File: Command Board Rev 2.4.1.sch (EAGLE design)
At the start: 44 parts, among them IC1 PIC24FXXKA302_SPDIP, Q2-IRF510 IRF740

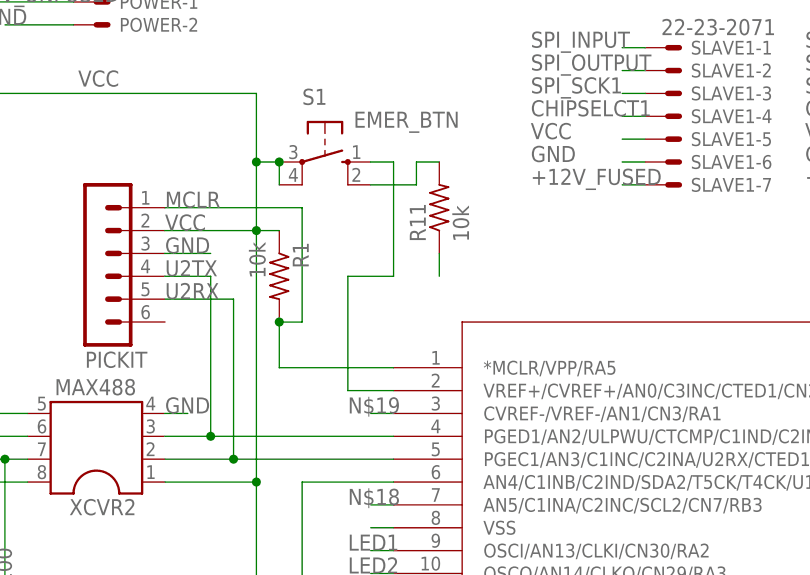
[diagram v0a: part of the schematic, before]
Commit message: Remove 2.4, Add 2.4.1
Replaces 2.4 files with 2.4.1
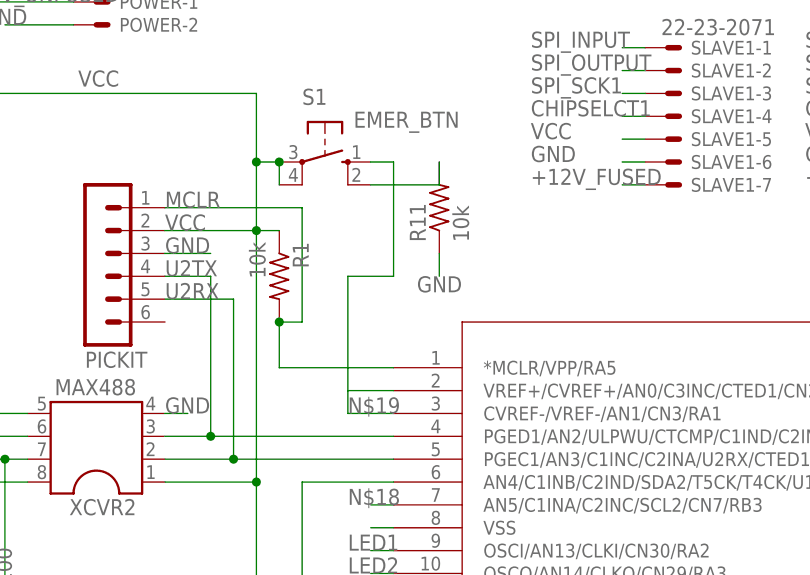
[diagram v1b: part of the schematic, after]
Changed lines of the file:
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@@
 <?xml version="1.0" encoding="utf-8"?>
 <!DOCTYPE eagle SYSTEM "eagle.dtd">
-<eagle version="7.4.0">
+<eagle version="7.7.0">
 <drawing>
 <settings>
@@
 <segment>
 <pinref part="IC1" gate="A" pin="VREF+/CVREF+/AN0/C3INC/CTED1/CN2/RA0"/>
-<pinref part="S1" gate="1" pin="S"/>
-<wire x1="198.12" y1="109.22" x2="200.66" y2="109.22" width="0.1524" layer="91"/>
 <wire x1="200.66" y1="109.22" x2="200.66" y2="96.52" width="0.1524" layer="91"/>
 <wire x1="200.66" y1="96.52" x2="195.58" y2="96.52" width="0.1524" layer="91"/>
 <wire x1="195.58" y1="96.52" x2="195.58" y2="83.82" width="0.1524" layer="91"/>
 <wire x1="195.58" y1="83.82" x2="200.66" y2="83.82" width="0.1524" layer="91"/>
+<pinref part="S1" gate="1" pin="S"/>
+<wire x1="198.12" y1="109.22" x2="200.66" y2="109.22" width="0.1524" layer="91"/>
 </segment>
 </net>
@@
 <pinref part="R11" gate="G$1" pin="1"/>
 <wire x1="205.74" y1="99.06" x2="205.74" y2="96.52" width="0.1524" layer="91"/>
+<label x="208.28" y="96.52" size="1.778" layer="95" rot="R180"/>
 </segment>
 <segment>
@@
 <segment>
 <pinref part="IC1" gate="A" pin="CVREF-/VREF-/AN1/CN3/RA1"/>
-<wire x1="200.66" y1="81.28" x2="198.12" y2="81.28" width="0.1524" layer="91"/>
 <label x="195.58" y="81.28" size="1.778" layer="95"/>
+<wire x1="200.66" y1="81.28" x2="195.58" y2="81.28" width="0.1524" layer="91"/>
+<wire x1="195.58" y1="81.28" x2="195.58" y2="83.82" width="0.1524" layer="91"/>
 </segment>
 </net>
@@
 <wire x1="228.6" y1="114.3" x2="226.06" y2="114.3" width="0.1524" layer="91"/>
 <label x="215.9" y="114.3" size="1.778" layer="95"/>
-</segment>
-</net>
-<net name="N$2" class="0">
-<segment>
-<pinref part="S1" gate="1" pin="S1"/>
-<wire x1="198.12" y1="106.68" x2="203.2" y2="106.68" width="0.1524" layer="91"/>
-<wire x1="203.2" y1="106.68" x2="203.2" y2="109.22" width="0.1524" layer="91"/>
-<pinref part="R11" gate="G$1" pin="2"/>
-<wire x1="203.2" y1="109.22" x2="205.74" y2="109.22" width="0.1524" layer="91"/>
 </segment>
 </net>
@@
 </segment>
 </net>
+<net name="N$2" class="0">
+<segment>
+<pinref part="S1" gate="1" pin="S1"/>
+<pinref part="R11" gate="G$1" pin="2"/>
+<wire x1="198.12" y1="106.68" x2="205.74" y2="106.68" width="0.1524" layer="91"/>
+<wire x1="205.74" y1="106.68" x2="205.74" y2="109.22" width="0.1524" layer="91"/>
+</segment>
+</net>
